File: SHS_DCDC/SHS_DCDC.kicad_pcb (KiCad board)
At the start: 4 copper layers, 100 x 100 mm, 101 parts, among them J1 Barrel_Jack, J2 USB_A, Q1 BSS84, Q10 PMV100XPEAR, Q11 PMV100XPEAR, Q12 PMV100XPEAR, Q13 PMV100XPEAR, Q14 2N7002, Q15 MOSP_GENERIC, Q16 MOSP_GENERIC, Q17 MOSP_GENERIC, Q2 PMV100XPEAR, Q3 2N7002, Q4 2N7002, Q5 PMV100XPEAR, Q6 2N7002, Q7 PMV100XPEAR, Q8 Q_PMOS_DGS, Q9 PMV100XPEAR, U1 RT8299-WDFN10L, U2 INA181, U3 LMV324AIDR, U4 LMV358IDR, U5 MP3414A, U6 ESP32-S2-MINI-1, U7 MCP101

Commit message: Ubuntu transfer
Commit before transfer onto Ubuntu
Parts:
- removed R46: 1k, Resistor_SMD:R_0603_1608Metric
- removed R47: 100k, Resistor_SMD:R_0402_1005Metric
- added C28: 100nF, Capacitor_SMD:C_0402_1005Metric, F.Cu at (15.0, 58.5)
- added C35: 100nF, Capacitor_SMD:C_0402_1005Metric, F.Cu at (-9.40, 44.9)
- added C36: 1uF, Capacitor_SMD:C_0402_1005Metric, F.Cu at (6.80, 68.0)
- added J3: Conn_ARM_JTAG_SWD_10, Connector_PinHeader_1.27mm:PinHeader_2x05_P1.27mm_Vertical, F.Cu at (15.0, 64.0)
- added R21: 10k, Resistor_SMD:R_0402_1005Metric, F.Cu at (5.60, 68.0)
- added S1: TS02-66-70-BK-160-LCR-D, Library:SW_TS02-66-70-BK-160-LCR-D, F.Cu at (9.10, 58.6)
- Q12: footprint digikey-footprints:SOT-23-3 -> digikey-kicad-library-master:SOT-23-3
- Q14: value 2N7002 -> PMV100XPEAR; footprint Package_TO_SOT_SMD:SOT-23 -> digikey-kicad-library-master:SOT-23-3
- Q15: value MOSP_GENERIC -> BSS84
- Q16, Q17: value MOSP_GENERIC -> PMV100XPEAR; footprint Package_TO_SOT_SMD:SOT-23 -> digikey-kicad-library-master:SOT-23-3
- R1: value R -> 100k
- moved Q14 133.6 mm to (92.9, -24.0)
- moved R16 82.3 mm to (57.3, 70.1), turned to 180 degrees
- moved Q17 39.6 mm to (123.4, 36.2)
- moved R1 14.5 mm to (106.0, -24.9)
- moved Q15 13.3 mm to (102.1, -23.7)
- moved R8 11.9 mm to (66.3, 62.3)
- moved Q16 4.42 mm to (88.2, -24.0)
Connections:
- J2 pad 2: Net-(J2-Pad2) -> USB_D-
- J2 pad 3: Net-(J2-Pad2) -> USB_D+
- Q14 pad 2: GND -> Net-(Q14-Pad2)
- Q14 pad 3: Net-(Q14-Pad3) -> Net-(C30-Pad1)
- Q15 pad 1: MCU_PVBAT_DIRECT -> MCU_MPPT_ENABLE
- Q15 pad 2: Net-(C30-Pad1) -> Net-(Q14-Pad1)
- Q15 pad 3: Net-(Q15-Pad3) -> GND
- Q16 pad 1: MCU_PVBAT_DIRECT -> Net-(Q14-Pad1)
- Q16 pad 2: DCDC_OUT -> Net-(Q14-Pad2)
- Q16 pad 3: Net-(Q15-Pad3) -> DCDC_OUT
- Q17 pad 2: Net-(R8-Pad1) -> VBAT
- Q17 pad 3: VBAT -> Net-(Q17-Pad3)
- R1 pad 1: Net-(Q15-Pad3) -> Net-(C30-Pad1)
- R1 pad 2: MCU_PVBAT_DIRECT -> Net-(Q14-Pad1)
- R48 pad 1: Net-(Q14-Pad1) -> MCU_MPPT_ENABLE
- R8 pad 1: Net-(R8-Pad1) -> Net-(Q17-Pad3)
- U1 pad 3: Net-(Q14-Pad3) -> MCU_MPPT_ENABLE
- U2 pad 3: Net-(R8-Pad1) -> Net-(Q17-Pad3)
- U6 pad 23: unconnected-(U6-Pad23) -> USB_D-
- U6 pad 24: unconnected-(U6-Pad24) -> USB_D+
- U6 pad 35: unconnected-(U6-Pad35) -> MCU_MTCK
- U6 pad 36: unconnected-(U6-Pad36) -> MCU_MTDO
- U6 pad 37: unconnected-(U6-Pad37) -> MCU_MTDI
- U6 pad 38: unconnected-(U6-Pad38) -> MCU_MTMS
- U6 pad 45: unconnected-(U6-Pad45) -> MCU_RST
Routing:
- net V_MCU: track 37.4 -> 52.0 mm
- net MCU_RST: track 0.00 -> 9.55 mm
- net Net-(R8-Pad1): track 8.62 -> 0.00 mm
- net Net-(Q17-Pad3): track 0.00 -> 6.12 mm
- net MCU_MTDI: track 0.00 -> 6.01 mm
- net MCU_MTMS: track 0.00 -> 5.98 mm, vias 0 -> 1
- net MCU_TL_ONOFFSIG: track 1.82 -> 7.80 mm
- net MCU_MTDO: track 0.00 -> 5.83 mm
- net MCU_MTCK: track 0.00 -> 5.66 mm
- net Net-(Q14-Pad3): track 2.68 -> 0.00 mm
- net MCU_MPPT_ENABLE: track 0.00 -> 2.68 mm
- net LOAD: track 21.0 -> 18.5 mm
- net Net-(J2-Pad2): track 2.00 -> 0.00 mm
- net GND: vias 0 -> 1

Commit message: Commit_190223
Normal commit
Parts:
- moved C8 118.1 mm to (33.8, 76.4), turned to -90 degrees
- moved Q15 105.2 mm to (39.0, 60.5)
- moved Q14 102.5 mm to (42.0, 65.0)
- moved Q16 95.4 mm to (44.0, 60.5)
- moved Q17 95.1 mm to (36.6, 75.0)
- moved C34 68.9 mm to (36.0, 47.7), turned to 90 degrees
- moved C33 64.2 mm to (34.3, 47.7), turned to 90 degrees
- moved U3 30.0 mm to (143.5, 33.6)
- moved R16 17.3 mm to (73.7, 64.6)
- moved R8 12.6 mm to (56.5, 70.2)
- moved R27 10.4 mm to (64.5, 33.0)
- moved Q7 10.1 mm to (64.5, 30.0)
- moved R20 10.0 mm to (41.5, 33.0)
- moved Q5 9.80 mm to (41.5, 30.0)
- moved R26 9.53 mm to (60.9, 36.0), turned to -90 degrees
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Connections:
- C23 pad 1: USB_IN -> LOAD
- L2 pad 2: USB_IN -> LOAD
- Q13 pad 1: unconnected-(Q13-Pad1) -> ODP_RESET
- R16 pad 1: OP_V1+ -> LOAD
- U3 pad 10: OP_V1+ -> LOAD
- U5 pad 1: USB_IN -> LOAD
- U6 pad 34: unconnected-(U6-Pad34) -> MCU_PWM_TL
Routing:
- net MCU_PWM_TL: track 0.00 -> 35.4 mm, vias 0 -> 2
- net LOAD_BULB2: track 54.3 -> 22.5 mm
- net LOAD: track 18.5 -> 0.04 mm
- net VBAT: track 40.2 -> 57.3 mm
- net LOAD_BULB1: track 31.6 -> 21.1 mm
- net Net-(Q4-Pad3): track 6.52 -> 0.00 mm
- net Net-(Q17-Pad3): track 6.12 -> 0.00 mm
- net Net-(Q6-Pad3): track 5.26 -> 0.00 mm
- net Net-(C17-Pad1): track 5.02 -> 0.00 mm
- net Net-(Q2-Pad1): track 6.50 -> 2.00 mm
- net ODP_RESET: track 0.00 -> 4.35 mm
- net Net-(C12-Pad1): track 4.32 -> 0.00 mm
- net Net-(C11-Pad1): track 3.87 -> 0.07 mm
- net (no net): track 3.38 -> 0.00 mm
- net Net-(C33-Pad1): track 1.76 -> 5.05 mm
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
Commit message: Commit_Fix
Fix to move back to ESP32
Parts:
- 4cells1: moved to F.Cu
- moved U7 109.5 mm to (57.5, 77.0), turned to -90 degrees
- moved U3 91.1 mm to (55.0, 55.0)
- moved Q14 29.7 mm to (26.0, 40.0), turned to 180 degrees
- moved C8 25.4 mm to (59.0, 79.7), turned to 0 degrees
- moved Q16 24.3 mm to (31.0, 40.0), turned to 180 degrees
- moved Q17 21.3 mm to (57.5, 71.0), turned to 90 degrees
- moved 4cells1 19.8 mm to (79.2, 57.5), turned to 0 degrees
- moved Q15 19.2 mm to (28.0, 44.7), turned to -90 degrees
- moved C6 7.30 mm to (46.0, 80.0)
- moved U2 7.30 mm to (50.0, 79.0)
- moved R8 6.50 mm to (50.0, 70.0)
- moved R26 1.90 mm to (59.0, 36.0)
- moved R19 1.80 mm to (36.1, 36.0)
- moved C17 1.70 mm to (60.7, 36.0)
- moved C12 1.60 mm to (37.8, 36.0)
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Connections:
- U6 pad 29: unconnected-(U6-Pad29) -> MCU_PWM_MPPT
- U6 pad 32: unconnected-(U6-Pad32) -> MCU_PWM_BL2
- U6 pad 33: unconnected-(U6-Pad33) -> MCU_PWM_BL1
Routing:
- net MCU_PWM_BL2: track 0.00 -> 70.8 mm, vias 0 -> 2
- net MCU_PWM_BL1: track 0.00 -> 48.0 mm, vias 0 -> 2
- net MCU_PWM_MPPT: track 1.60 -> 40.1 mm
- net DCDC_OUT: track 10.0 -> 42.5 mm, vias 2 -> 0
- net VBAT: track 57.3 -> 46.8 mm
- net Net-(Q17-Pad3): track 0.00 -> 8.55 mm
- net LOAD: track 0.04 -> 8.59 mm
- net Net-(C30-Pad1): track 0.00 -> 8.24 mm
- net Net-(Q14-Pad1): track 0.00 -> 7.85 mm
- net MCU_MPPT_ENABLE: track 2.68 -> 9.09 mm
- net Net-(Q14-Pad2): track 0.00 -> 5.00 mm
- net VREF_BIDIRECTIONAL: track 21.6 -> 24.6 mm, vias 2 -> 0
- net Net-(C32-Pad1): track 2.63 -> 1.53 mm
- added copper zone on F.Cu, net Net-(Q17-Pad3)

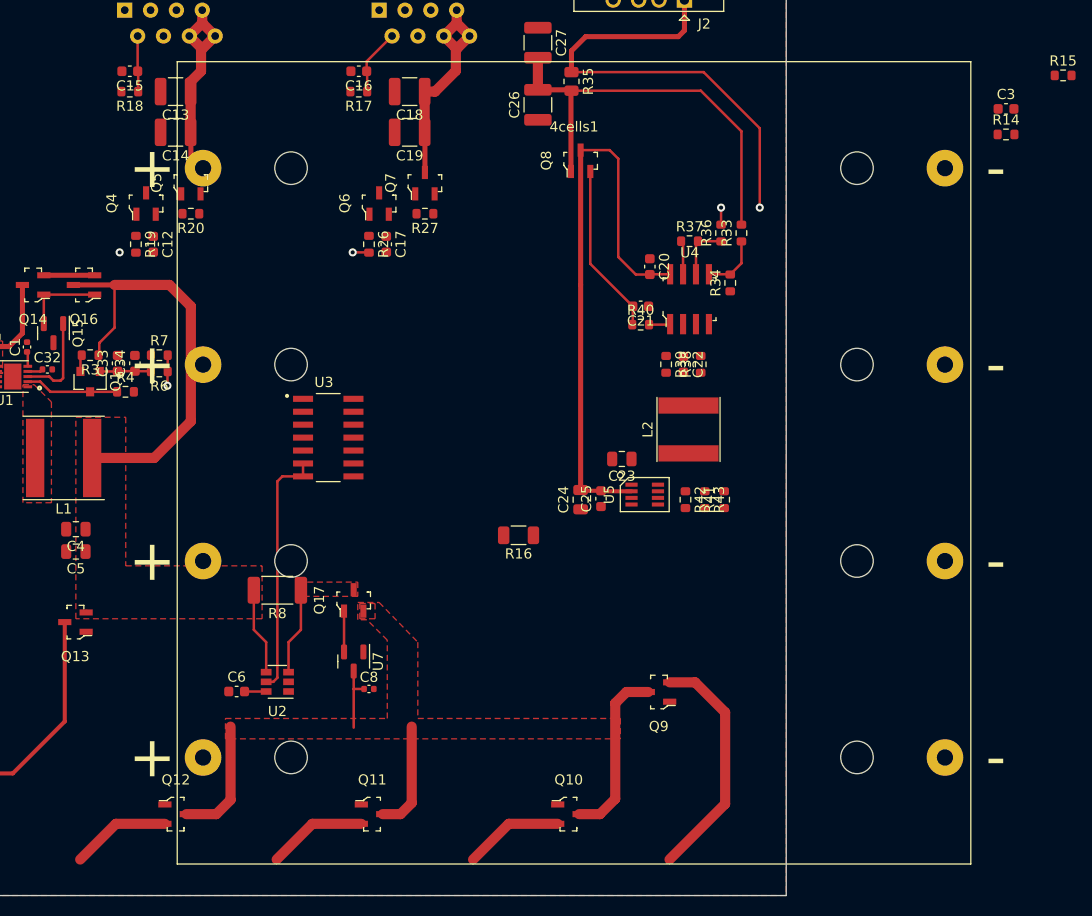
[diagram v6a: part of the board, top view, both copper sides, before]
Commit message: Commit010323
Progress on the USB current limitation
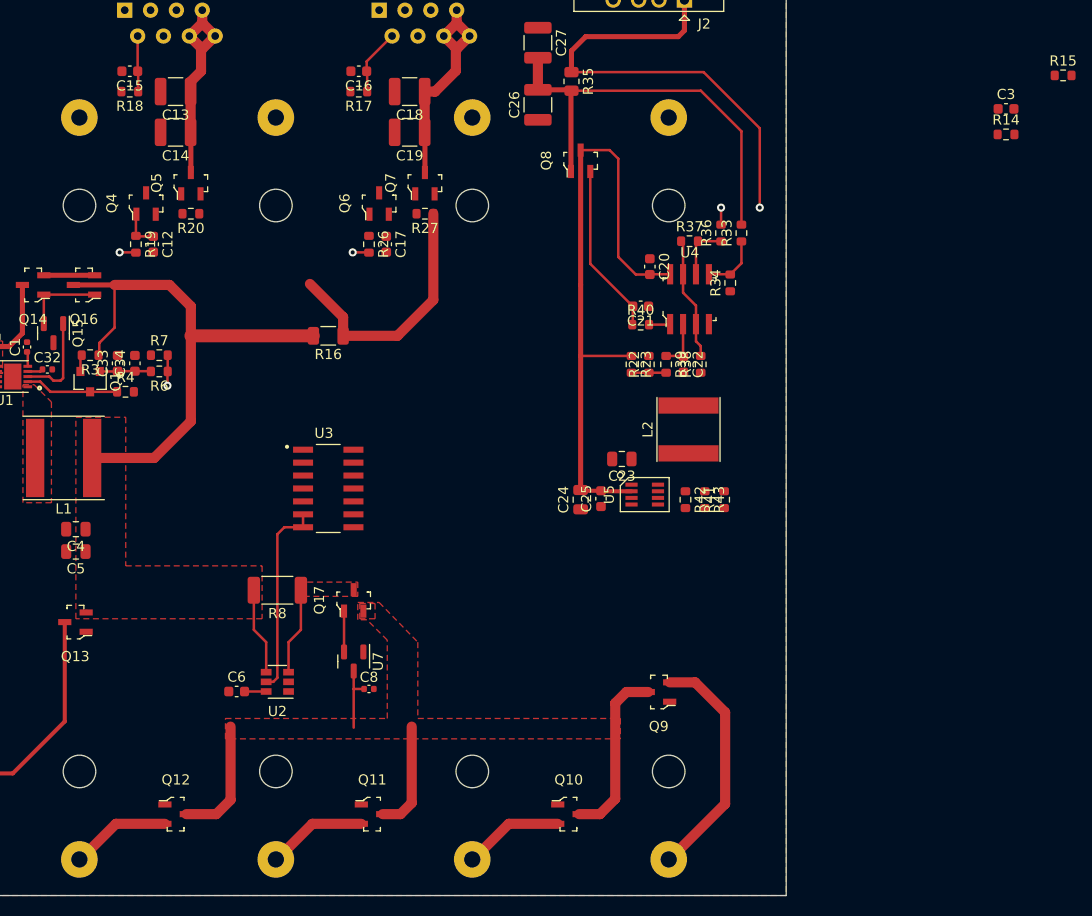
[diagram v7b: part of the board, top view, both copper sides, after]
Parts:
- added R22: 25k, Resistor_SMD:R_0603_1608Metric, F.Cu at (86.5, 47.8)
- added R23: 100k, Resistor_SMD:R_0603_1608Metric, F.Cu at (84.8, 47.8)
- 4cells1: moved to B.Cu
- R35: value R -> TBD
- moved R16 27.1 mm to (55.0, 45.0)
- moved 4cells1 19.8 mm to (59.5, 60.0), turned to 90 degrees
- moved U3 5.00 mm to (55.0, 60.0)
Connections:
- J2 pad 1: Net-(J2-Pad1) -> Net-(C26-Pad2)
- Q8 pad 1: Net-(C26-Pad2) -> Net-(Q8-Pad1)
- R33 pad 2: Net-(C26-Pad2) -> Net-(Q8-Pad1)
- R35 pad 1: Net-(J2-Pad1) -> Net-(C26-Pad2)
- R35 pad 2: Net-(C26-Pad2) -> Net-(Q8-Pad1)
- R36 pad 2: Net-(J2-Pad1) -> Net-(C26-Pad2)
- R39 pad 2: ILIM_USB -> MCU_ILIM_USB
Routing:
- net Net-(J2-Pad1): track 51.1 -> 0.00 mm, vias 2 -> 0
- net Net-(Q8-Pad1): track 0.00 -> 42.0 mm
- net LOAD: track 8.59 -> 33.8 mm
- net DCDC_OUT: track 42.5 -> 54.5 mm
- net Net-(C26-Pad2): track 42.0 -> 51.1 mm, vias 0 -> 2
- net I_USB: track 3.33 -> 12.1 mm
- net VREF_BIDIRECTIONAL: track 24.6 -> 19.4 mm
- net 5V: track 58.0 -> 63.0 mm
- net Net-(C22-Pad1): track 0.00 -> 4.91 mm
- net Net-(C12-Pad1): track 0.00 -> 3.87 mm
- net MCU_ILIM_USB: track 0.00 -> 3.40 mm
- net MCU_PWM_BL1: track 48.0 -> 49.6 mm

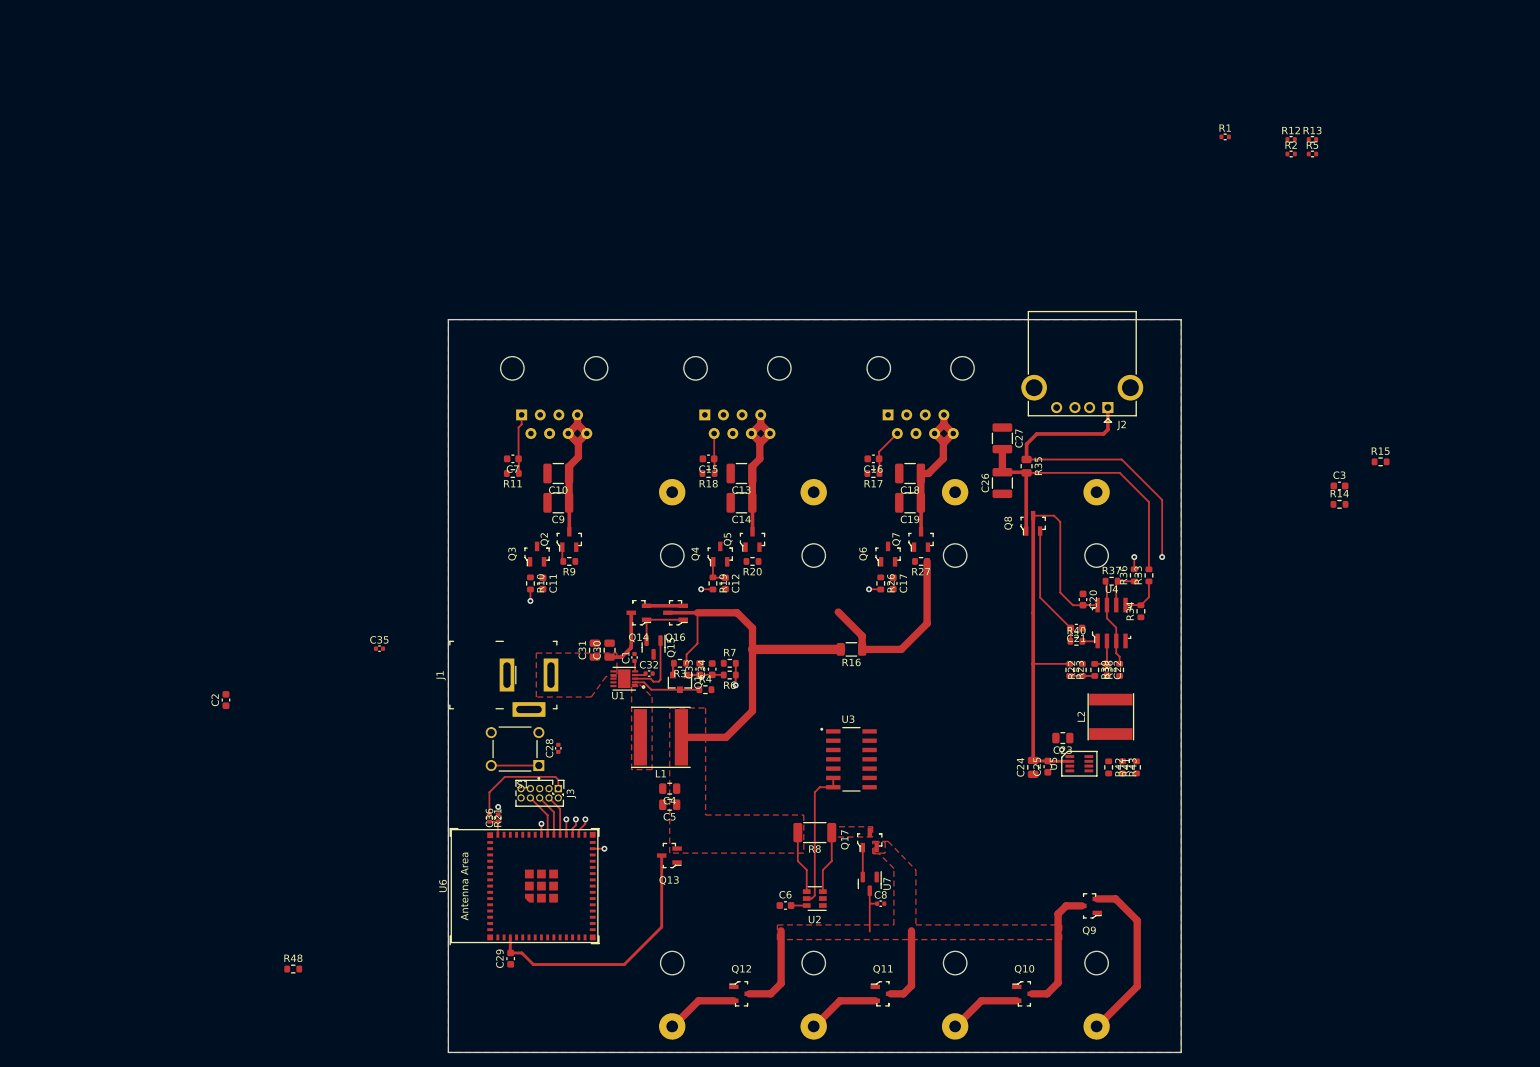
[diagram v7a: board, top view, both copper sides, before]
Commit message: Error fix on DCDC block
Wrong pinout on DCDC block that needed to be fixed
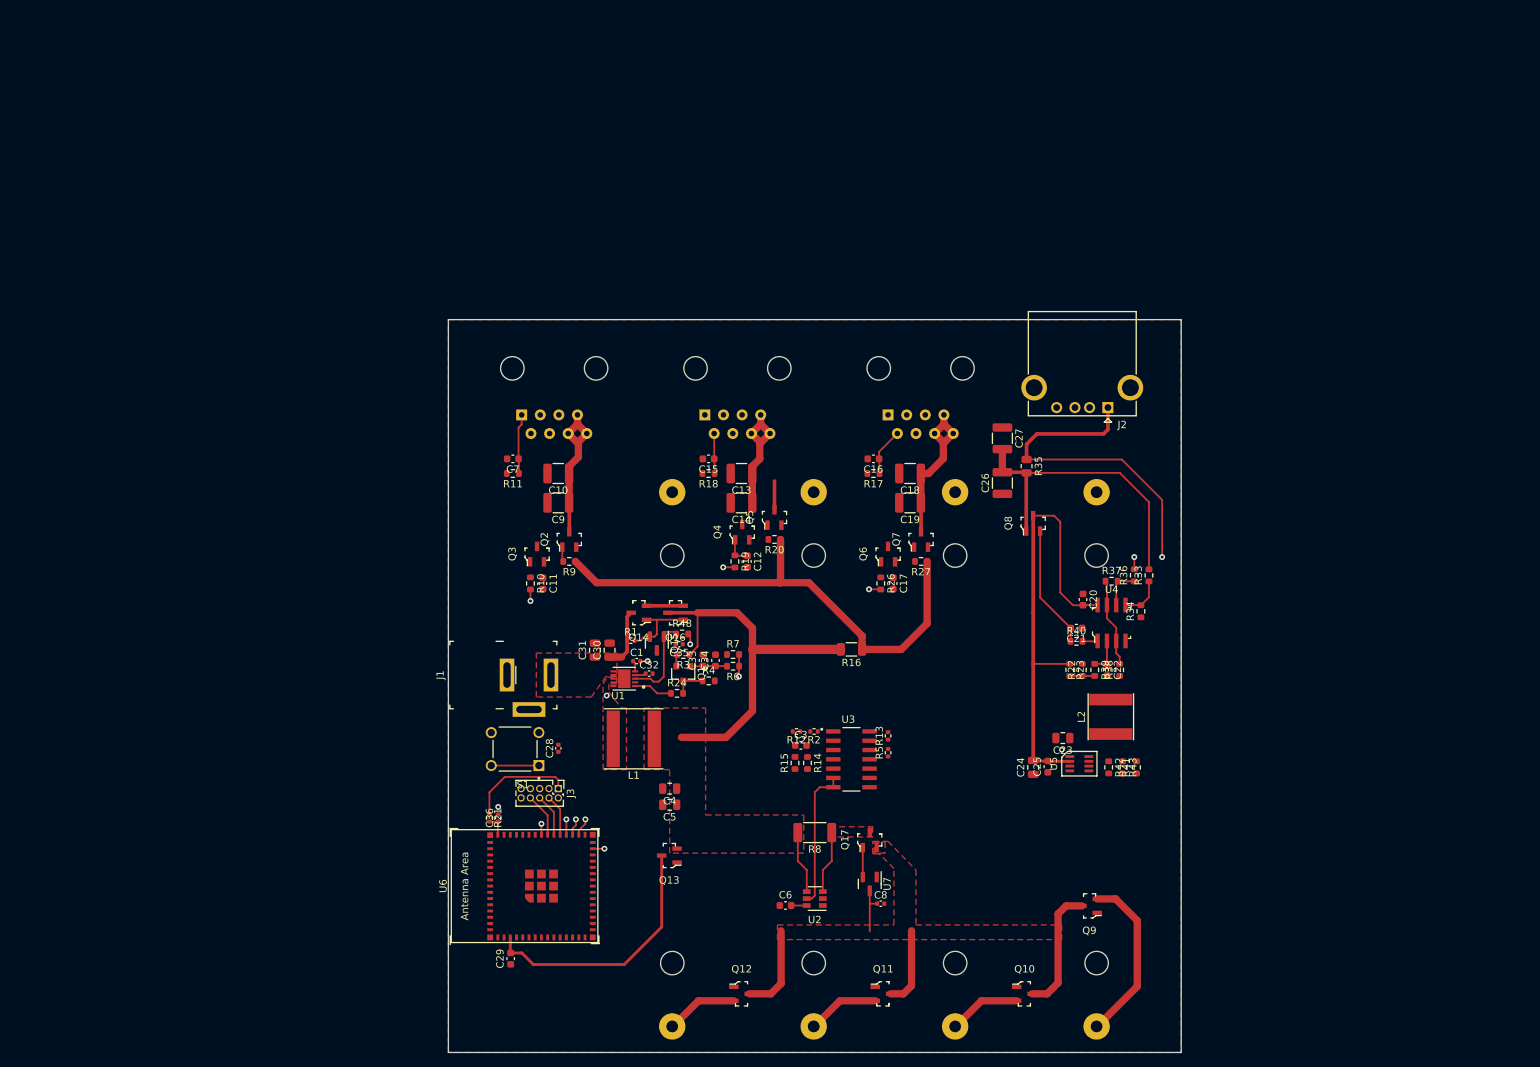
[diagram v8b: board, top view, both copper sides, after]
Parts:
- removed C2: 100nF, Capacitor_SMD:C_0603_1608Metric
- added R24: R, Resistor_SMD:R_0603_1608Metric, F.Cu at (31.2, 51.0)
- moved R1 106.3 mm to (24.9, 43.8)
- moved R12 105.3 mm to (47.5, 56.2), turned to 180 degrees
- moved R2 102.2 mm to (49.9, 56.2), turned to 180 degrees
- moved R5 100.1 mm to (60.0, 59.1), turned to 90 degrees
- moved R13 99.9 mm to (60.0, 56.8), turned to 90 degrees
- moved R15 89.9 mm to (47.3, 60.5), turned to 90 degrees
- moved C3 81.6 mm to (48.1, 58.1)
- moved R14 80.7 mm to (49.0, 60.5), turned to -90 degrees
- moved R48 70.0 mm to (31.9, 42.9)
- moved C35 40.9 mm to (31.5, 44.3), turned to 180 degrees
- moved C12 4.24 mm to (40.8, 33.0)
- moved Q4 4.24 mm to (40.1, 29.0)
- moved Q5 4.24 mm to (44.5, 27.0)
- moved R19 4.24 mm to (39.1, 33.0)
- moved R20 4.24 mm to (44.5, 30.0)
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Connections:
- C1 pad 2: GND -> Net-(L1-Pad2)
- L1 pad 2: Net-(C2-Pad2) -> Net-(L1-Pad2)
- U1 pad 1: Net-(C2-Pad2) -> Net-(U1-Pad1)
- U1 pad 2: Net-(Q1-Pad3) -> unconnected-(U1-Pad2)
- U1 pad 8: Net-(C2-Pad1) -> Net-(L1-Pad2)
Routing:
- net LOAD: track 33.8 -> 78.5 mm
- net Net-(L1-Pad2): track 0.00 -> 10.6 mm, vias 0 -> 2
- net Net-(U1-Pad1): track 0.00 -> 5.31 mm
- net Net-(Q1-Pad3): track 9.19 -> 4.36 mm
- net MCU_MPPT_ENABLE: track 9.09 -> 13.7 mm
- net MCU_PWM_BL1: track 49.6 -> 53.9 mm
- net Net-(Q14-Pad1): track 7.85 -> 10.4 mm
- net GND: track 0.00 -> 1.51 mm, vias 1 -> 2
- net DCDC_OUT: track 54.5 -> 53.2 mm
- added copper zone on F.Cu, net Net-(L1-Pad2)
- removed copper zone on F.Cu, net Net-(C2-Pad2)
